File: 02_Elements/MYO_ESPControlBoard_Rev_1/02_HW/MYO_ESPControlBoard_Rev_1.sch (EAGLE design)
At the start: 55 parts, among them X1 USB-MICROB

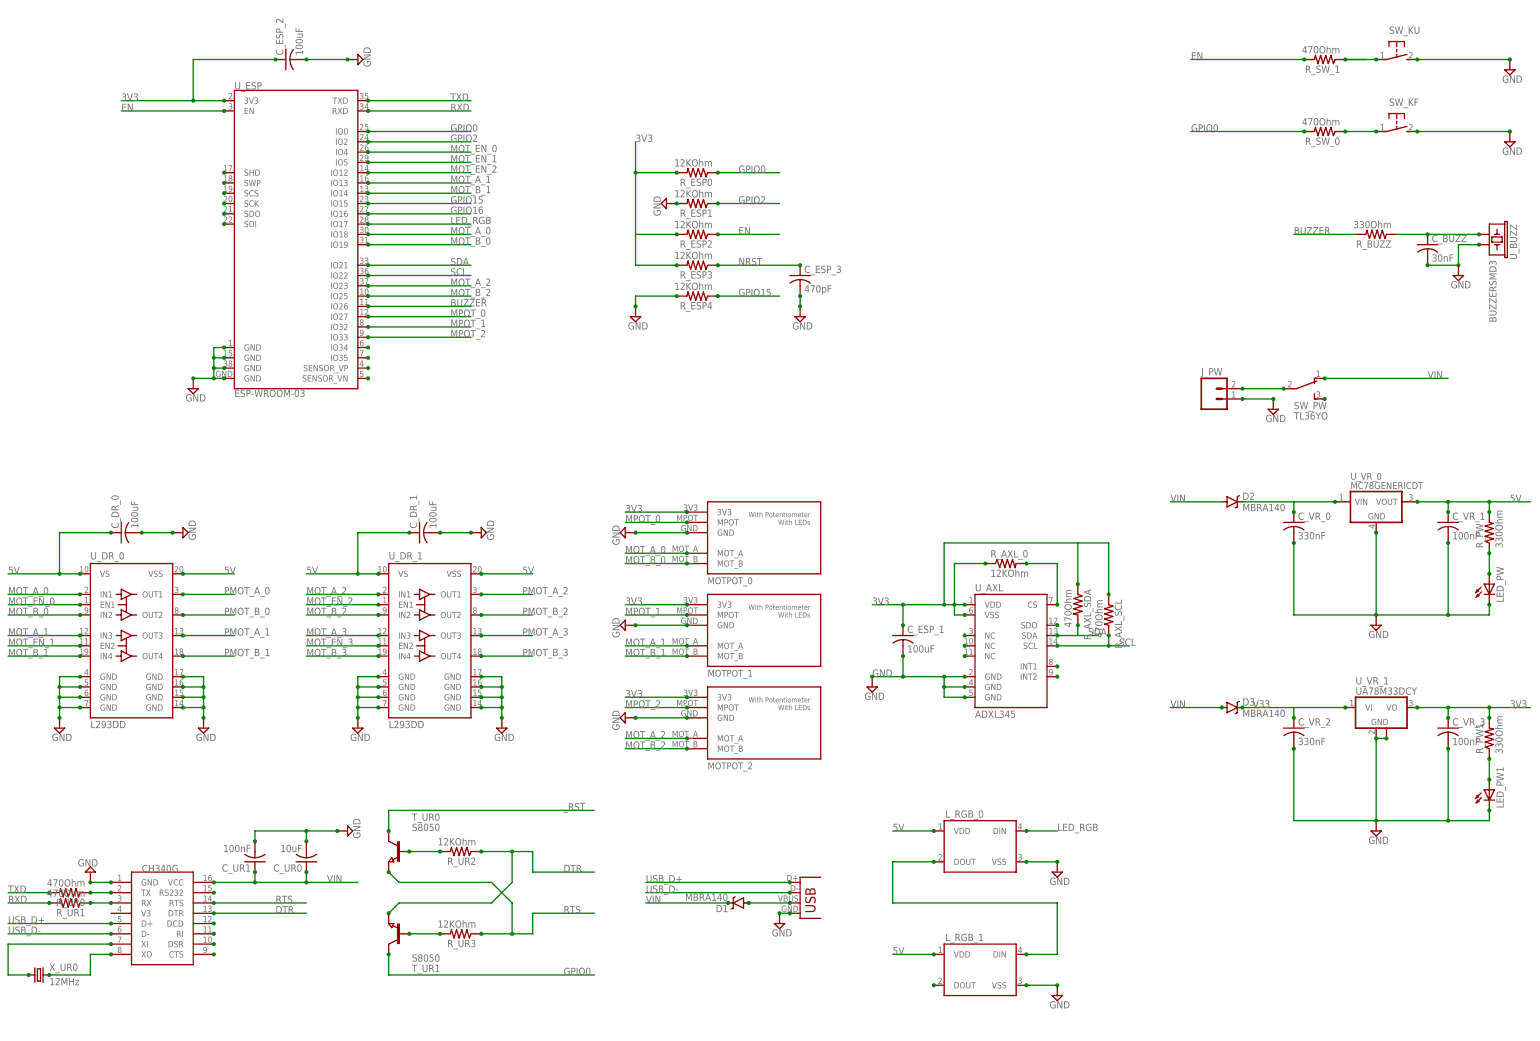
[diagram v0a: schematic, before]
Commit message: MYO_ESPControlBoard_Rev_1 Draft Update on HW (SCH, BRD and 3D)
Primary Draft of the PCB Schematic and Layout of MYO_ESPControlBoard_Rev_1, for evaluation:

- Complete Schematic
- Draft Layout without Drills or Silk
- Primary 3D Model
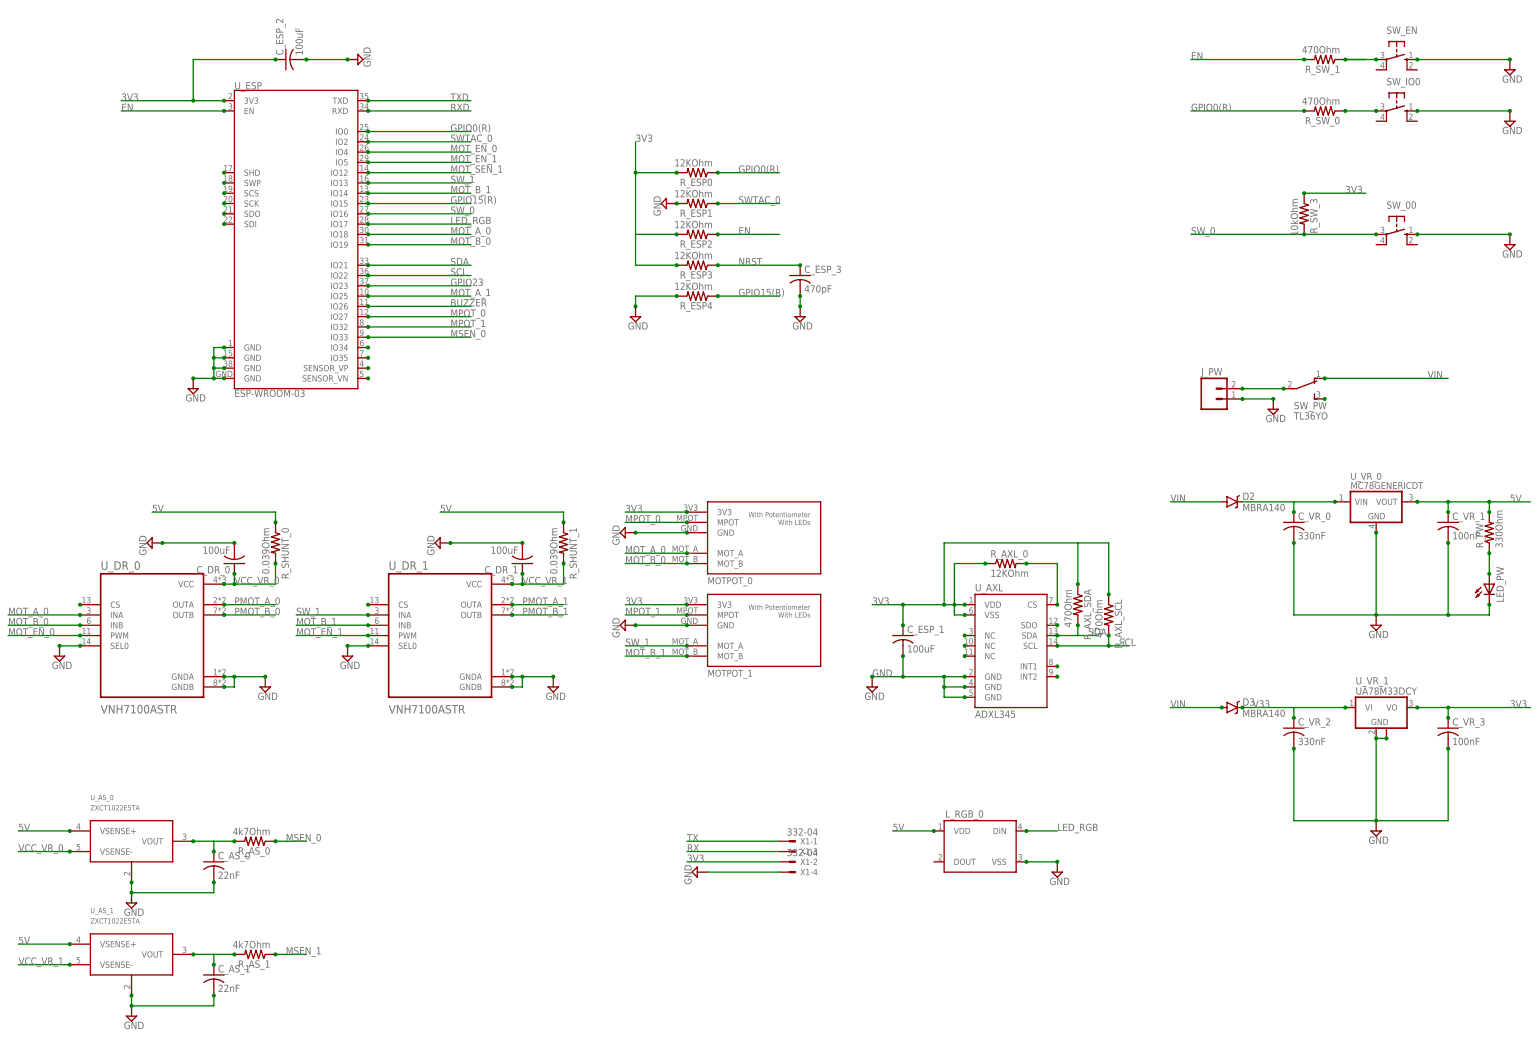
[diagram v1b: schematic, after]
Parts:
- removed C_BUZZ: 30nF, adafruit:C-USC0805K
- removed C_UR0: 10uF, adafruit:C-USC0805K
- removed C_UR1: 100nF, adafruit:C-USC0805K
- removed D1: MBRA140, SparkFun-DiscreteSemi:MBRA140
- removed LED_PW1: (no value), adafruit:LEDSMT1206
- removed L_RGB_1: (no value), SparkFun-LED:WS2812B
- removed MOTPOT_2: POLOLU_MOT_POT, PololuMotors:POLOLU_MOT_POT
- removed R_BUZZ, R_PW1: 330Ohm, adafruit:R-US_M0805
- removed R_UR0, R_UR1: 470Ohm, adafruit:R-US_M0805
- removed R_UR2, R_UR3: 12KOhm, adafruit:R-US_M0805
- removed SW_KF, SW_KU: (no value), switch-omron:31-XX
- removed T_UR0, T_UR1: S8050, semicon-smd-ipc:NPN-TRANSISTOR_SOT23
- removed U_BUZZ: BUZZERSMD3, SparkFun:BUZZERSMD3
- removed U_UR0: CH340G, ch340g:CH340G
- removed X_UR0: 12MHz, adafruit:CRYSTALCTS406
- added C_AS_0, C_AS_1: 22nF, adafruit:C-USC0805K
- added R_AS_0, R_AS_1: 4k7Ohm, adafruit:R-US_M0805
- added R_SHUNT_0, R_SHUNT_1: 0.039Ohm, adafruit:R-US_M0805
- added R_SW_3: 10kOhm, adafruit:R-US_M0805
- added SW_00, SW_EN, SW_IO0: (no value), switch-omron:10-XX
- added U_AS_0, U_AS_1: ZXCT1022E5TA, ZXCT1022E5TA:ZXCT1022E5TA
- U_DR_0, U_DR_1: value L293DD -> VNH7100ASTR; device st-microelectronics:L293DD -> VNH7100ASTR:VNH7100ASTR
- X1: value USB-MICROB -> 332-04; device SparkFun:USB-MICROB -> con-garry:332-04
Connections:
- net GPIO15 renamed GPIO15(R)
- net GPIO2 renamed SWTAC_0
- removed net DTR: R_UR2.1, T_UR1.E, U_UR0.DTR
- removed net GPIO0: R_ESP0.1, R_SW_0.2, T_UR1.C, U_ESP.IO0
- removed net GPIO16: U_ESP.IO16
- removed net MOT_A_2: MOTPOT_2.MOT_A, U_DR_1.IN1, U_ESP.IO23
- removed net MOT_A_3: U_DR_1.IN3
- removed net MOT_B_2: MOTPOT_2.MOT_B, U_DR_1.IN2, U_ESP.IO25
- removed net MOT_B_3: U_DR_1.IN4
- removed net MOT_EN_2: U_DR_1.EN1, U_ESP.IO12
- removed net MOT_EN_3: U_DR_1.EN2
- removed net MPOT_2: MOTPOT_2.MPOT, U_ESP.IO33
- removed net N$10: L_RGB_0.DOUT, L_RGB_1.DIN
- removed net N$12: R_UR0.1, U_UR0.TX
- removed net N$13: R_UR1.1, U_UR0.RX
- removed net N$14: U_UR0.XO, X_UR0.2
- removed net N$15: D1.A, X1.VBUS
- removed net N$2: U_UR0.RS232
- removed net N$3: R_UR3.2, T_UR1.B
- removed net N$37: U_UR0.CTS
- removed net N$38: U_UR0.RI
- removed net N$39: U_UR0.DSR
- removed net N$4: R_UR2.2, T_UR0.B
- removed net N$40: U_UR0.DCD
- removed net N$7: U_UR0.XI, X_UR0.1
- removed net N$8: LED_PW1.A, R_PW1.1
- removed net N$9: L_RGB_1.DOUT
- removed net PMOT_A_2: U_DR_1.OUT1
- removed net PMOT_A_3: U_DR_1.OUT3
- removed net PMOT_B_2: U_DR_1.OUT2
- removed net PMOT_B_3: U_DR_1.OUT4
- removed net RTS: R_UR3.1, T_UR0.E, U_UR0.RTS
- removed net USB_D+: U_UR0.D+, X1.D+
- removed net USB_D-: U_UR0.D-, X1.D-
- removed net _RST: T_UR0.C
- new net GPIO0(R): R_ESP0.1, R_SW_0.2, U_ESP.IO0
- new net GPIO23: U_ESP.IO23
- new net MOT_SEN_1: U_ESP.IO12
- new net MSEN_0: R_AS_0.1, U_ESP.IO33
- new net MSEN_1: R_AS_1.1
- new net N$11: C_AS_0.1, R_AS_0.2, U_AS_0.VOUT
- new net N$42: C_AS_1.1, R_AS_1.2, U_AS_1.VOUT
- new net N$6: U_DR_1.CS
- new net RX: X1-3.S
- new net SW_0: R_SW_3.2, SW_00.P, U_ESP.IO16
- new net SW_1: MOTPOT_1.MOT_A, U_DR_1.INA, U_ESP.IO13
- new net TX: X1-1.S
- new net VCC_VR_0: C_DR_0.1, R_SHUNT_0.2, R_SHUNT_1.2, U_AS_0.VSENSE-, U_DR_0.VCC
- new net VCC_VR_1: C_DR_1.1, U_AS_1.VSENSE-, U_DR_1.VCC
- net 3V3: now also R_SW_3.1, X1-2.S; no longer MOTPOT_2.3V3, R_PW1.2
- net 5V: now also R_SHUNT_0.1, R_SHUNT_1.1, U_AS_0.VSENSE+, U_AS_1.VSENSE+; no longer C_DR_0.1, C_DR_1.1, L_RGB_1.VDD, U_DR_0.VS, U_DR_0.VSS, U_DR_1.VS, U_DR_1.VSS
- net BUZZER: no longer R_BUZZ.2
- net GND: now also C_AS_0.2, C_AS_1.2, SW_00.S, SW_EN.S, SW_IO0.S, U_AS_0.GND, U_AS_1.GND, U_DR_0.GNDA, U_DR_0.GNDB, U_DR_0.SEL0, U_DR_1.GNDA, U_DR_1.GNDB, U_DR_1.SEL0, X1-4.S; no longer C_BUZZ.2, C_UR0.2, C_UR1.2, LED_PW1.C, L_RGB_1.VSS, MOTPOT_2.GND, SW_KF.S, SW_KU.S, U_BUZZ.2, U_DR_0.GND@1, U_DR_0.GND@2, U_DR_0.GND@3, U_DR_0.GND@4, U_DR_0.GND@5, U_DR_0.GND@6, U_DR_0.GND@7, U_DR_0.GND@8, U_DR_1.GND@1, U_DR_1.GND@2, U_DR_1.GND@3, U_DR_1.GND@4, U_DR_1.GND@5, U_DR_1.GND@6, U_DR_1.GND@7, U_DR_1.GND@8, U_UR0.GND, X1.GND
- net MOT_A_0: now also U_DR_0.INA; no longer U_DR_0.IN1
- net MOT_A_1: now also U_ESP.IO25; no longer MOTPOT_1.MOT_A, U_DR_0.IN3, U_ESP.IO13
- net MOT_B_0: now also U_DR_0.INB; no longer U_DR_0.IN2
- net MOT_B_1: now also U_DR_1.INB; no longer U_DR_0.IN4
- net MOT_EN_0: now also U_DR_0.PWM; no longer U_DR_0.EN1
- net MOT_EN_1: now also U_DR_1.PWM; no longer U_DR_0.EN2
- net N$1: now also U_DR_0.CS; no longer C_BUZZ.1, R_BUZZ.1, U_BUZZ.1
- net N$18: now also SW_EN.P; no longer SW_KU.P
- net N$19: now also SW_IO0.P; no longer SW_KF.P
- net PMOT_A_0: now also U_DR_0.OUTA; no longer U_DR_0.OUT1
- net PMOT_A_1: now also U_DR_1.OUTA; no longer U_DR_0.OUT3
- net PMOT_B_0: now also U_DR_0.OUTB; no longer U_DR_0.OUT2
- net PMOT_B_1: now also U_DR_1.OUTB; no longer U_DR_0.OUT4
- net RXD: no longer R_UR1.2
- net TXD: no longer R_UR0.2
- net VIN: no longer C_UR0.1, C_UR1.1, D1.C, U_UR0.VCC
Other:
- note added: "CURRENT SENSOR: Linear Operation up to: Vsense = (Vin - 2)/100 = 30mV Vout = 100 x Vsense Vout MAX = 4V @Vin=5V Vsense mac ) = 40mV @Vin=5V R SHUNT CALCULATION: Vsense = 40mV @Isense = 1A Rshunt = Vsense * Isense = 0.040R Max Motor Current = 1.6A Absolute maz Vsense = 500mV Max Power dissipated by Rshunt = 100mW"
- note added: "GPIO/PIN: GPIO4 GPIO18 GPIO19 GPIO27 GPIO5 GPIO25 GPIO14 GPIO32 GPIO12 GPIO33 GPIO17 GPIO16 GPIO13 GPIO21 GPIO22"
- note added: "Motor Current Sensors"
- note added: "SW Programming Interface"
- note added: "SW Switch Interface"
- note added: "Signal: MOT_EN_0 MOT_A_0 MOT_B_0 MPOT_0 MOT_EN_1 MOT_A_1 MOT_B_1 MPOT_1 MSEN_0 MSEN_1 LED_RGB SW_0 SW_1 SDA SCL"
- note removed: "Buzzer Circuit"
- note removed: "GPIO/PIN: GPIO4 GPIO18 GPIO19 GPIO27 GPIO5 GPIO13 GPIO14 GPIO32 GPIO12 GPIO23 GPIO25 GPIO33 GPIO17 GPIO26 GPIO21 GPIO22"
- note removed: "SW Interface"
- note removed: "Signal: MOT_EN_0 MOT_A_0 MOT_B_0 MPOT_0 MOT_EN_1 MOT_A_1 MOT_B_1 MPOT_1 MOT_EN_2 MOT_A_2 MOT_B_2 MPOT_2 LED_RGB BUZZER SDA SCL"
- moved on the sheet: C_DR_0, C_DR_1, R_SW_0

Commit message: Updated Design with NPN JTAG Programming Interface
Changed Schematic:

- Added NPN JTAG Controller (as for https://dl.espressif.com/dl/schematics/ESP32-Core-Board-V2_sch.pdf ). Suppresed 2 Tactile Switches for Programming Interface
- Added 1 Tactile Switch for User Interface
- Added Expressiv Documentation
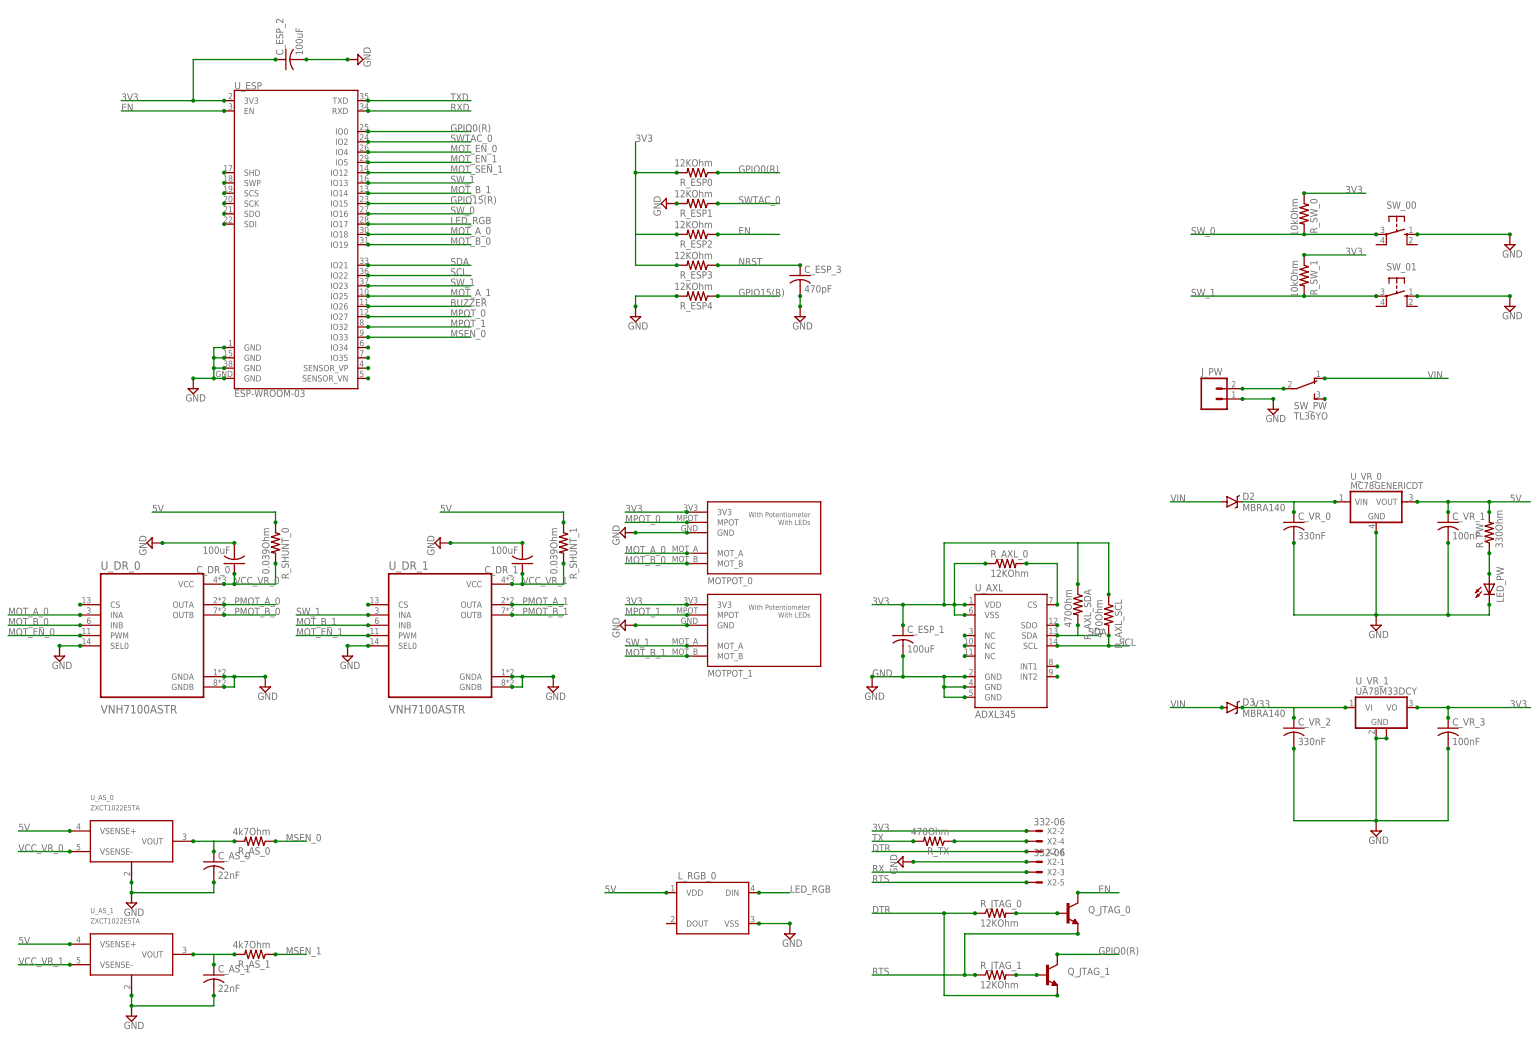
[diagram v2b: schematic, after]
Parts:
- removed R_SW_3: 10kOhm, adafruit:R-US_M0805
- removed SW_EN, SW_IO0: (no value), switch-omron:10-XX
- removed X1: 332-04, con-garry:332-04
- added Q_JTAG_0, Q_JTAG_1: (no value), SparkFun:TRANSISTOR_NPNSOT23-3
- added R_JTAG_0, R_JTAG_1: 12KOhm, adafruit:R-US_M0805
- added R_TX: 470Ohm, adafruit:R-US_M0805
- added SW_01: (no value), switch-omron:10-XX
- added X2: 332-06, con-garry:332-06
- R_SW_0, R_SW_1: value 470Ohm -> 10kOhm
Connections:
- removed net GPIO23: U_ESP.IO23
- removed net N$18: R_SW_1.1, SW_EN.P
- removed net N$19: R_SW_0.1, SW_IO0.P
- new net DTR: Q_JTAG_1.E, R_JTAG_0.1, X2-6.S
- new net N$4: Q_JTAG_0.B, R_JTAG_0.2
- new net N$7: Q_JTAG_1.B, R_JTAG_1.2
- new net N$9: R_TX.1, X2-4.S
- new net RTS: Q_JTAG_0.E, R_JTAG_1.1, X2-5.S
- net 3V3: now also R_SW_0.1, R_SW_1.1, X2-2.S; no longer R_SW_3.1, X1-2.S
- net EN: now also Q_JTAG_0.C; no longer R_SW_1.2
- net GND: now also SW_01.S, X2-1.S; no longer SW_EN.S, SW_IO0.S, X1-4.S
- net GPIO0(R): now also Q_JTAG_1.C; no longer R_SW_0.2
- net RX: now also X2-3.S; no longer X1-3.S
- net SW_0: now also R_SW_0.2; no longer R_SW_3.2
- net SW_1: now also R_SW_1.2, SW_01.P, U_ESP.IO23
- net TX: now also R_TX.2; no longer X1-1.S
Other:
- note removed: "SW Programming Interface"
- moved on the sheet: L_RGB_0, R_SW_0, R_SW_1

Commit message: MYO_ESPControlBoard_Rev_1 Schematic Fixed. New Dimensions for Board
MYO_ESPControlBoard_Rev_1:

- Schematic Fixed
- Tactile Switch SW_1 Removed
- New Dimensions and Board Layout

Transition Commit, soon to be finished :-)
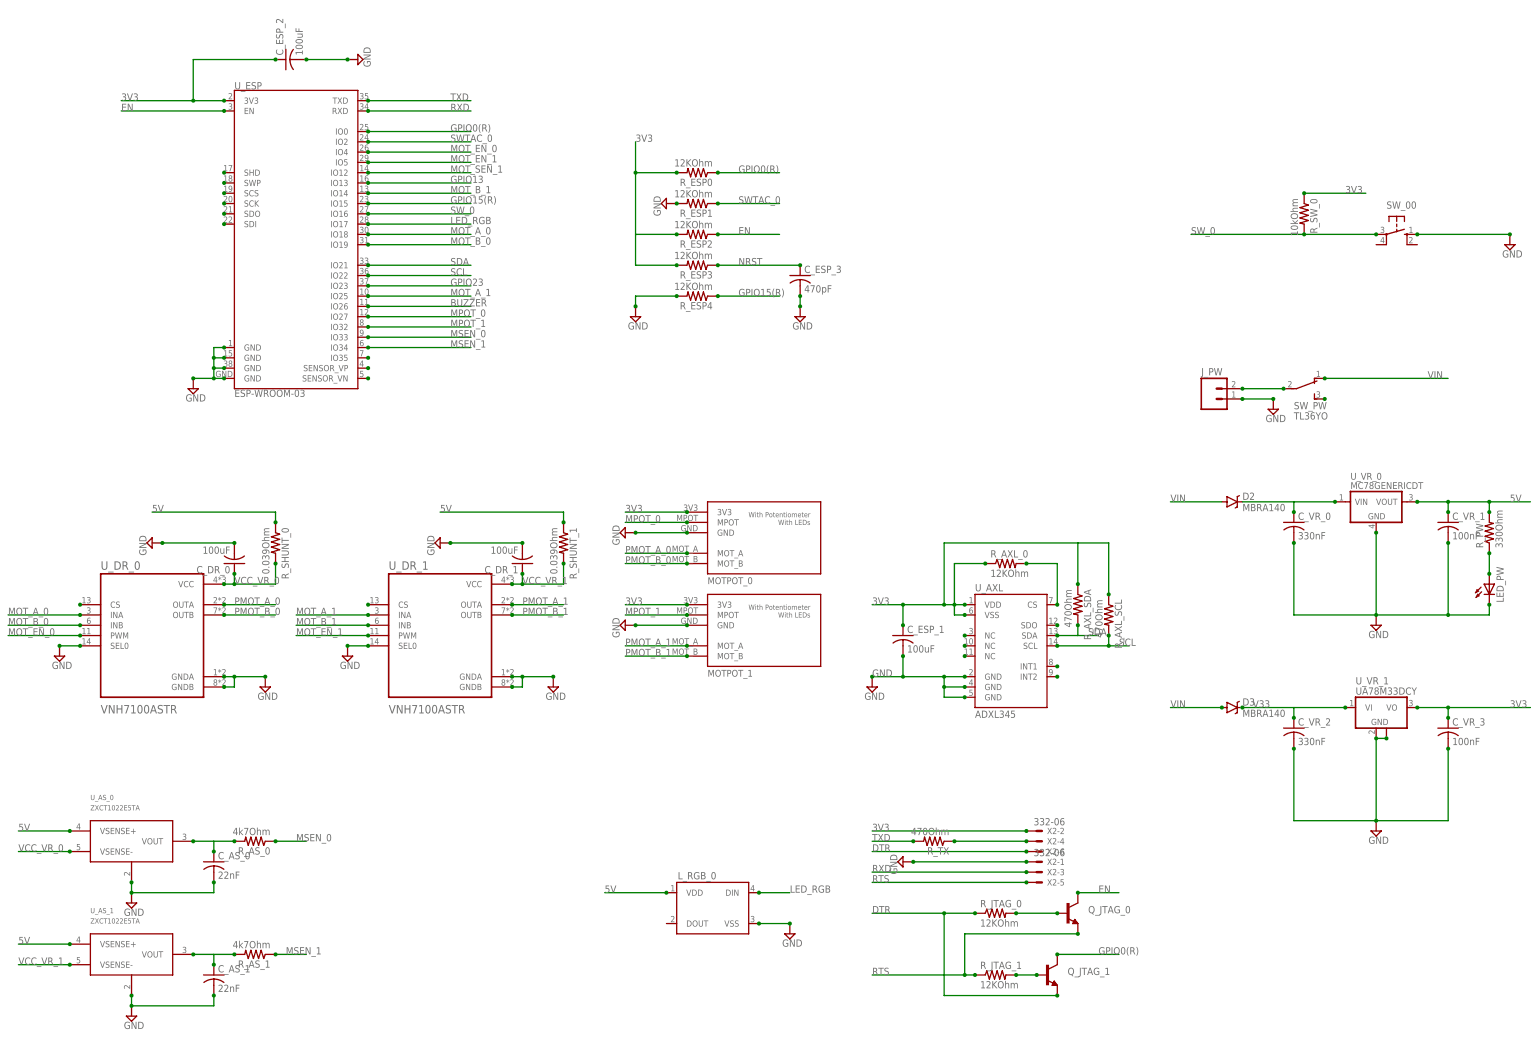
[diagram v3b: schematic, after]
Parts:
- removed R_SW_1: 10kOhm, adafruit:R-US_M0805
- removed SW_01: (no value), switch-omron:10-XX
- R_PW: device adafruit:R-US_M1206 -> adafruit:R-US_M0805
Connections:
- removed net N$32: U_ESP.IO34
- removed net RX: X2-3.S
- removed net SW_1: MOTPOT_1.MOT_A, R_SW_1.2, SW_01.P, U_DR_1.INA, U_ESP.IO13, U_ESP.IO23
- removed net TX: R_TX.2
- new net GPIO13: U_ESP.IO13
- new net GPIO23: U_ESP.IO23
- net 3V3: no longer R_SW_1.1
- net GND: no longer SW_01.S
- net MOT_A_0: no longer MOTPOT_0.MOT_A
- net MOT_A_1: now also U_DR_1.INA
- net MOT_B_0: no longer MOTPOT_0.MOT_B
- net MOT_B_1: no longer MOTPOT_1.MOT_B
- net MSEN_1: now also U_ESP.IO34
- net PMOT_A_0: now also MOTPOT_0.MOT_A
- net PMOT_A_1: now also MOTPOT_1.MOT_A
- net PMOT_B_0: now also MOTPOT_0.MOT_B
- net PMOT_B_1: now also MOTPOT_1.MOT_B
- net RXD: now also X2-3.S
- net TXD: now also R_TX.2
- net VCC_VR_0: no longer R_SHUNT_1.2
- net VCC_VR_1: now also R_SHUNT_1.2
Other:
- note added: "GPIO/PIN: GPIO4 GPIO18 GPIO19 GPIO27 GPIO5 GPIO25 GPIO14 GPIO32 GPIO12 GPIO33 GPIO17 GPIO16 GPIO21 GPIO22"
- note added: "Signal: MOT_EN_0 MOT_A_0 MOT_B_0 MPOT_0 MOT_EN_1 MOT_A_1 MOT_B_1 MPOT_1 MSEN_0 MSEN_1 LED_RGB SW_0 SDA SCL"
- note removed: "GPIO/PIN: GPIO4 GPIO18 GPIO19 GPIO27 GPIO5 GPIO25 GPIO14 GPIO32 GPIO12 GPIO33 GPIO17 GPIO16 GPIO13 GPIO21 GPIO22"
- note removed: "Signal: MOT_EN_0 MOT_A_0 MOT_B_0 MPOT_0 MOT_EN_1 MOT_A_1 MOT_B_1 MPOT_1 MSEN_0 MSEN_1 LED_RGB SW_0 SW_1 SDA SCL"
